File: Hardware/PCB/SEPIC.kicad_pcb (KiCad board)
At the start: 2 copper layers, 33.6 x 35.9 mm, 27 parts, among them Q1 IRF7807, U1 LM3478MA

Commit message: Finished PCB layout
A few minor adjustments still need to be made
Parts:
- added G***: LOGO, Logo_footprint:Logo_10_6, B.Cu at (124.3, 65.1)
- added G***: LOGO, Logo_footprint:Logo_15_15, B.Cu at (110.5, 65.2)
- moved R1 45.6 mm to (99.9, 75.8), turned to 90 degrees
- moved R7 43.7 mm to (124.3, 52.6), turned to 180 degrees
- moved R6 43.0 mm to (119.1, 54.7), turned to 180 degrees
- moved U1 42.5 mm to (124.3, 57.9), turned to 90 degrees
- moved C7 41.9 mm to (120.4, 58.9), turned to -90 degrees
- moved C2 40.7 mm to (105.9, 73.8), turned to -90 degrees
- moved L2 38.1 mm to (118.7, 65.1), turned to -90 degrees
- moved D1 38.0 mm to (99.9, 71.1), turned to 90 degrees
- moved Q1 37.3 mm to (123.3, 74.9), turned to 0 degrees
- moved R4 36.3 mm to (124.1, 69.3)
- moved C1 35.5 mm to (117.9, 58.9), turned to -90 degrees
- moved C5 34.8 mm to (116.8, 70.0), turned to 0 degrees
- moved L1 34.1 mm to (115.0, 74.9), turned to 90 degrees
- moved D4 33.5 mm to (112.3, 67.6), turned to -90 degrees
- moved R2 32.8 mm to (107.9, 64.8), turned to -90 degrees
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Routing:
- net GND: track 0.00 -> 92.7 mm, vias 0 -> 47
- net /Feedback: track 0.00 -> 24.7 mm
- net /DR: track 0.00 -> 23.5 mm, vias 0 -> 2
- net /Isen: track 0.00 -> 20.5 mm, vias 0 -> 2
- net Vin: track 0.00 -> 9.77 mm, vias 0 -> 2
- net Net-(R3-Pad2): track 0.00 -> 7.91 mm
- net Net-(Q1-D): track 0.00 -> 6.24 mm
- net Net-(U1-FA/SD): track 0.00 -> 3.17 mm
- net Net-(U1-COMP): track 0.00 -> 2.88 mm
- net Net-(C6-Pad1): track 0.00 -> 2.41 mm
- net Net-(U1-V_{IN}): track 0.00 -> 2.17 mm
- net Net-(D3-K): track 0.00 -> 1.90 mm
- net Net-(D1-K): track 0.00 -> 1.88 mm
- added copper zone on B.Cu, net GND
- added copper zone on F.Cu, net GND
- added copper zone on F.Cu, net Net-(D4-A)
- added copper zone on F.Cu, net Vin
- added copper zone on F.Cu, net Vout
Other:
- board size 33.6 x 35.9 mm -> 37.5 x 28.5 mm
- board text added: "Boost/Buck DC/DC converter |10/10/2026|"
- board text added: "Vin"
- board text added: "Vin : 3-20 V Vout : 3-20 V Max I : 3 A const."
- board text added: "Vout"

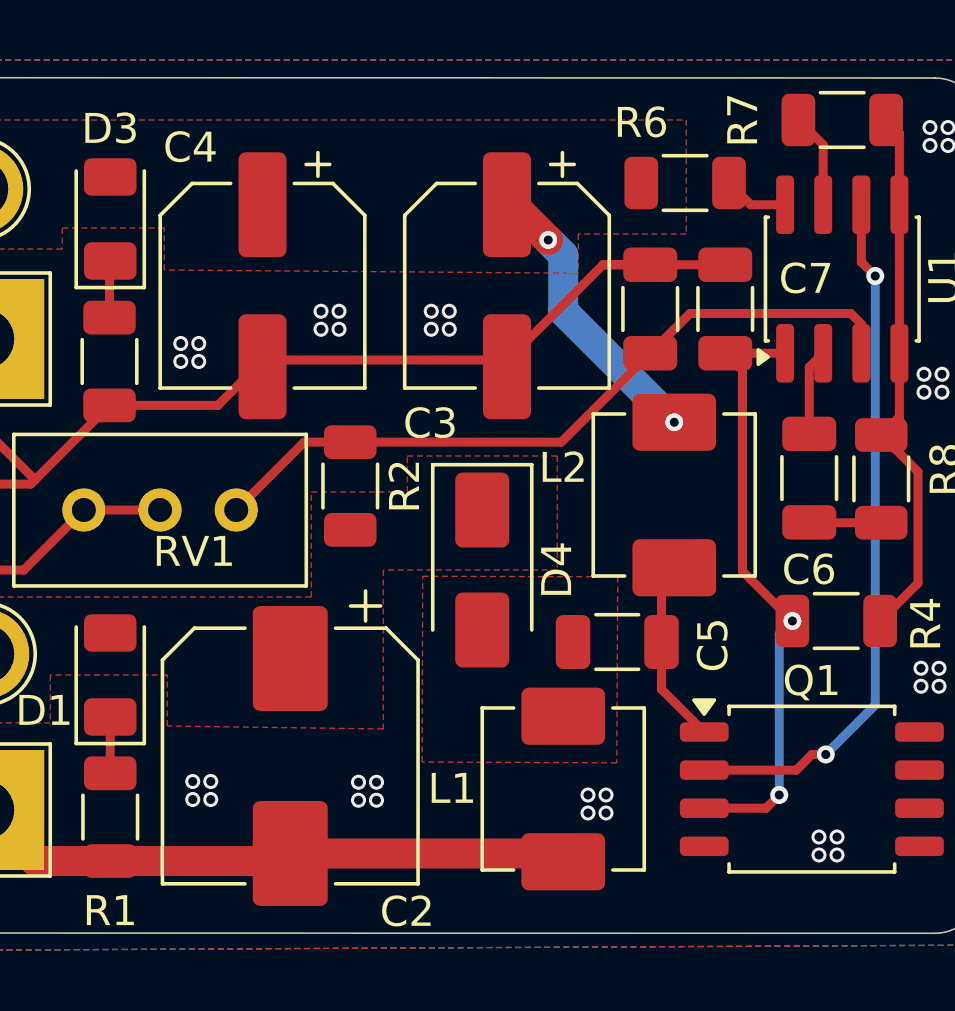
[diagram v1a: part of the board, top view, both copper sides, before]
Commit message: Add C8; update footprints, routing, schematic
Added capacitor C8 (1206) to PCB and schematic and created Hardware/PCB/SEPIC.png. Updated many footprint positions, silk labels and power symbols (#PWR17), adjusted routing (new segments, vias, some trace widths increased), and refined filled copper polygons. Schematic updated with new wires/junctions and an embedded board image. Also changed project prefs (active_layer) and recorded used_designators in .kicad_pro.
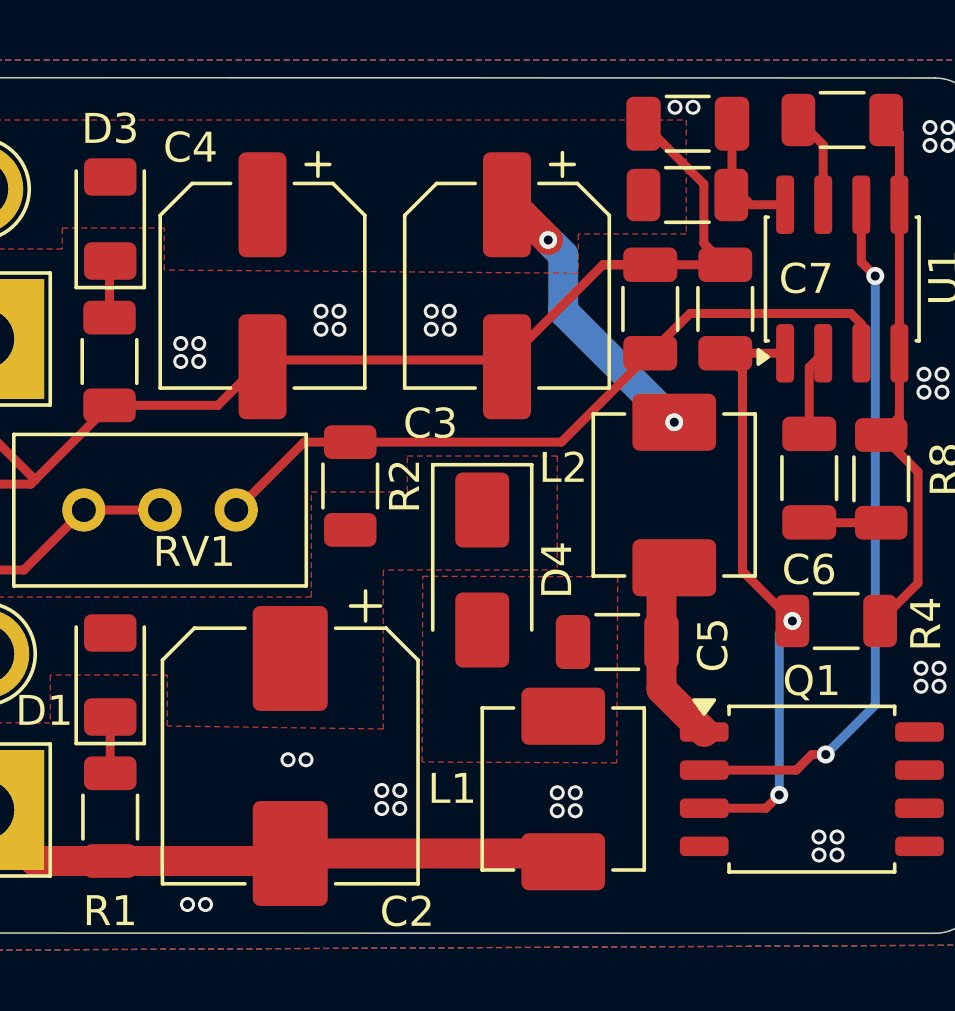
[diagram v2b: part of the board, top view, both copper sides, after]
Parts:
- added C8: 100p, Capacitor_SMD:C_1206_3216Metric, F.Cu at (119.2, 52.7)
- moved G*** 1.92 mm to (112.1, 64.0)
- moved R6 0.41 mm to (119.1, 55.1)
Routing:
- net GND: track 92.7 -> 98.5 mm, vias 47 -> 49
- net Net-(U1-V_{IN}): track 2.17 -> 4.56 mm
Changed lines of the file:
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@@
 		)
 	)
+	(footprint "Capacitor_SMD:C_1206_3216Metric"
+		(layer "F.Cu")
+		(at 119.15 52.725 180)
+		(descr "Capacitor SMD 1206 (3216 Metric), square (rectangular) end terminal, IPC-7351 nominal, (Body size source: IPC-SM-782 page 76, https://www.pcb-3d.com/wordpress/wp-content/uploads/ipc-sm-782a_amendment_1_and_2.pdf)")
+		(tags "capacitor")
+		(property "Reference" "C8"
+			(at -3.1 0.275 270)
+			(layer "B.SilkS")
+			(effects
+				(font
+					(size 1 1)
+					(thickness 0.15)
+				)
+				(justify mirror)
+			)
+		)
+		(property "Value" "100p"
+			(at 0 1.85 0)
+			(layer "F.Fab")
+			(effects
+				(font
+					(size 1 1)
+					(thickness 0.15)
+				)
+			)
+		)
+		(property "Datasheet" ""
+			(at 0 0 0)
+			(layer "F.Fab")
+			(hide yes)
+			(effects
+				(font
+					(size 1.27 1.27)
+				)
+			)
+		)
+		(property "Description" "Unpolarized capacitor"
+			(at 0 0 0)
+			(layer "F.Fab")
+			(hide yes)
+			(effects
+				(font
+					(size 1.27 1.27)
+				)
+			)
+		)
+		(property "KiLib_Generator" "SMD_2terminal_chip_molded"
+			(at 0 0 0)
+			(layer "F.SilkS")
+			(hide yes)
+			(effects
+				(font
+					(size 1 1)
+					(thickness 0.15)
+				)
+			)
+		)
+		(property ki_fp_filters "C_*")
+		(sheetname "/")
+		(sheetfile "SEPIC.kicad_sch")
+		(units
+			(unit
+				(name "A")
+				(pins "1" "2")
+			)
+		)
+		(attr smd)
+		(duplicate_pad_numbers_are_jumpers no)
+		(fp_line
+			(start -0.711252 0.91)
+			(end 0.711252 0.91)
+			(stroke
+				(width 0.12)
+				(type solid)
+			)
+			(layer "F.SilkS")
+		)
+		(fp_line
+			(start -0.711252 -0.91)
+			(end 0.711252 -0.91)
+			(stroke
+				(width 0.12)
+				(type solid)
+			)
+			(layer "F.SilkS")
+		)
+		(fp_rect
+			(start -2.3 -1.15)
+			(end 2.3 1.15)
+			(stroke
+				(width 0.05)
+				(type solid)
+			)
+			(fill no)
+			(layer "F.CrtYd")
+		)
+		(fp_rect
+			(start -1.6 -0.8)
+			(end 1.6 0.8)
+			(stroke
+				(width 0.1)
+				(type solid)
+			)
+			(fill no)
+			(layer "F.Fab")
+		)
+		(fp_text user "${REFERENCE}"
+			(at 0 0 0)
+			(layer "F.Fab")
+			(effects
+				(font
+					(size 0.8 0.8)
+					(thickness 0.12)
+				)
+			)
+		)
+		(pad "1" smd roundrect
+			(at -1.475 0 180)
+			(size 1.15 1.8)
+			(layers "F.Cu" "F.Mask" "F.Paste")
+			(roundrect_rratio 0.217391)
+			(net "Net-(U1-V_{IN})")
+			(pintype "passive")
+		)
+		(pad "2" smd roundrect
+			(at 1.475 0 180)
+			(size 1.15 1.8)
+			(layers "F.Cu" "F.Mask" "F.Paste")
+			(roundrect_rratio 0.217391)
+			(net "GND")
+			(pintype "passive")
+		)
+		(embedded_fonts no)
+		(model "${KICAD10_3DMODEL_DIR}/Capacitor_SMD.3dshapes/C_1206_3216Metric.step"
+			(offset
+				(xyz 0 0 0)
+			)
+			(scale
+				(xyz 1 1 1)
+			)
+			(rotate
+				(xyz 0 0 0)
+			)
+		)
+	)
 	(footprint "Inductor_SMD:L_Vishay_IHLP-2020"
 		(layer "F.Cu")
@@
 		(tags "resistor")
 		(property "Reference" "R7"
-			(at 3.3 0 90)
-			(layer "F.SilkS")
+			(at -1.4 -1.75 180)
+			(layer "B.SilkS")
 			(effects
 				(font
@@
 					(thickness 0.15)
 				)
+				(justify mirror)
 			)
 		)
@@
 	(footprint "Resistor_SMD:R_1206_3216Metric"
 		(layer "F.Cu")
-		(at 119.0625 54.7 180)
+		(at 119.1375 55.1 180)
 		(descr "Resistor SMD 1206 (3216 Metric), square (rectangular) end terminal, IPC-7351 nominal, (Body size source: IPC-SM-782 page 72, https://www.pcb-3d.com/wordpress/wp-content/uploads/ipc-sm-782a_amendment_1_and_2.pdf)")
 		(tags "resistor")
 		(property "Reference" "R6"
-			(at 1.4625 2 0)
-			(layer "F.SilkS")
+			(at -1.0875 -1 180)
+			(layer "B.SilkS")
 			(effects
 				(font
@@
 					(thickness 0.15)
 				)
+				(justify mirror)
 			)
 		)
@@
 		(tags "capacitor")
 		(property "Reference" "C1"
-			(at 0 -0.1 0)
+			(at -0.15 -2.35 0)
 			(layer "B.SilkS")
 			(effects
@@
 	(footprint "Logo_footprint:Logo_15_15"
 		(layer "B.Cu")
-		(at 110.5 65.15 -90)
+		(at 112.075 64.05 -90)
 		(property "Reference" "G***"
 			(at 0 0 90)
@@
 		)
 	)
-	(gr_text "Vin		: 	3-20 V\nVout	:	3-20 V\nMax I	: 	3 A const."
+	(gr_text "Vin		: 	3-20 V\nVout	:	3-20 V\nMax I	:  3 A const."
 		(at 110.775 76.025 0)
 		(layer "B.SilkS" knockout)
@@
 	)
 	(segment
+		(start 119.6875 56.7125)
+		(end 120.4 57.425)
+		(width 0.3)
+		(layer "F.Cu")
+		(net "GND")
+	)
+	(segment
 		(start 94.5 64.7375)
 		(end 97.25 64.7375)
@@
 	)
 	(segment
+		(start 119.6875 54.7375)
+		(end 119.6875 56.7125)
+		(width 0.3)
+		(layer "F.Cu")
+		(net "GND")
+	)
+	(segment
+		(start 117.675 52.725)
+		(end 119.6875 54.7375)
+		(width 0.3)
+		(layer "F.Cu")
+		(net "GND")
+	)
+	(segment
 		(start 95.7 62.9)
 		(end 95.7 59.9)
@@
 	)
 	(via
-		(at 116.425 75.7)
+		(at 115.4 75.625)
 		(size 0.5)
 		(drill 0.3)
@@
 	)
 	(via
-		(at 108.175 74.675)
+		(at 108.95 74.95)
 		(size 0.5)
 		(drill 0.3)
@@
 	)
 	(via
-		(at 103.25 74.65)
+		(at 106.425 73.925)
 		(size 0.5)
 		(drill 0.3)
@@
 	)
 	(via
+		(at 119.325 52.175)
+		(size 0.5)
+		(drill 0.3)
+		(layers "F.Cu" "B.Cu")
+		(net "GND")
+	)
+	(via
 		(at 127.025 61.675)
 		(size 0.5)
@@
 	)
 	(via
-		(at 116.425 75.1)
+		(at 115.4 75.025)
 		(size 0.5)
 		(drill 0.3)
@@
 	)
 	(via
-		(at 108.775 74.675)
+		(at 109.55 74.95)
 		(size 0.5)
 		(drill 0.3)
@@
 	)
 	(via
-		(at 102.65 75.25)
+		(at 102.475 78.75)
 		(size 0.5)
 		(drill 0.3)
@@
 	)
 	(via
-		(at 115.825 75.7)
+		(at 114.8 75.625)
 		(size 0.5)
 		(drill 0.3)
@@
 	)
 	(via
-		(at 108.175 75.275)
+		(at 108.95 75.55)
 		(size 0.5)
 		(drill 0.3)
@@
 	)
 	(via
-		(at 102.65 74.65)
+		(at 105.825 73.925)
 		(size 0.5)
 		(drill 0.3)
@@
 	)
 	(via
-		(at 115.825 75.1)
+		(at 118.725 52.175)
+		(size 0.5)
+		(drill 0.3)
+		(layers "F.Cu" "B.Cu")
+		(net "GND")
+	)
+	(via
+		(at 114.8 75.025)
 		(size 0.5)
 		(drill 0.3)
@@
 	)
 	(via
-		(at 103.25 75.25)
+		(at 103.075 78.75)
 		(size 0.5)
 		(drill 0.3)
@@
 	)
 	(via
-		(at 108.775 75.275)
+		(at 109.55 75.55)
 		(size 0.5)
 		(drill 0.3)
@@
 		(start 118.275 71.575)
 		(end 119.7 73)
-		(width 0.3)
+		(width 1)
 		(layer "F.Cu")
 		(net "Net-(Q1-D)")
@@
 		(start 118.275 70)
 		(end 118.275 67.9505)
-		(width 0.3)
+		(width 1)
 		(layer "F.Cu")
 		(net "Net-(Q1-D)")
@@
 		(start 118.275 70)
 		(end 118.275 71.575)
-		(width 0.3)
+		(width 1)
 		(layer "F.Cu")
 		(net "Net-(Q1-D)")
@@
 	)
 	(segment
+		(start 120.625 52.725)
+		(end 120.625 55.075)
+		(width 0.3)
+		(layer "F.Cu")
+		(net "Net-(U1-V_{IN})")
+	)
+	(segment
 		(start 122.395 55.425)
 		(end 121.25 55.425)
 		(width 0.3)
 		(layer "F.Cu")
+		(net "Net-(U1-V_{IN})")
+	)
+	(segment
+		(start 120.625 55.075)
+		(end 120.6 55.1)
+		(width 0.3)
+		(layer "F.Cu")

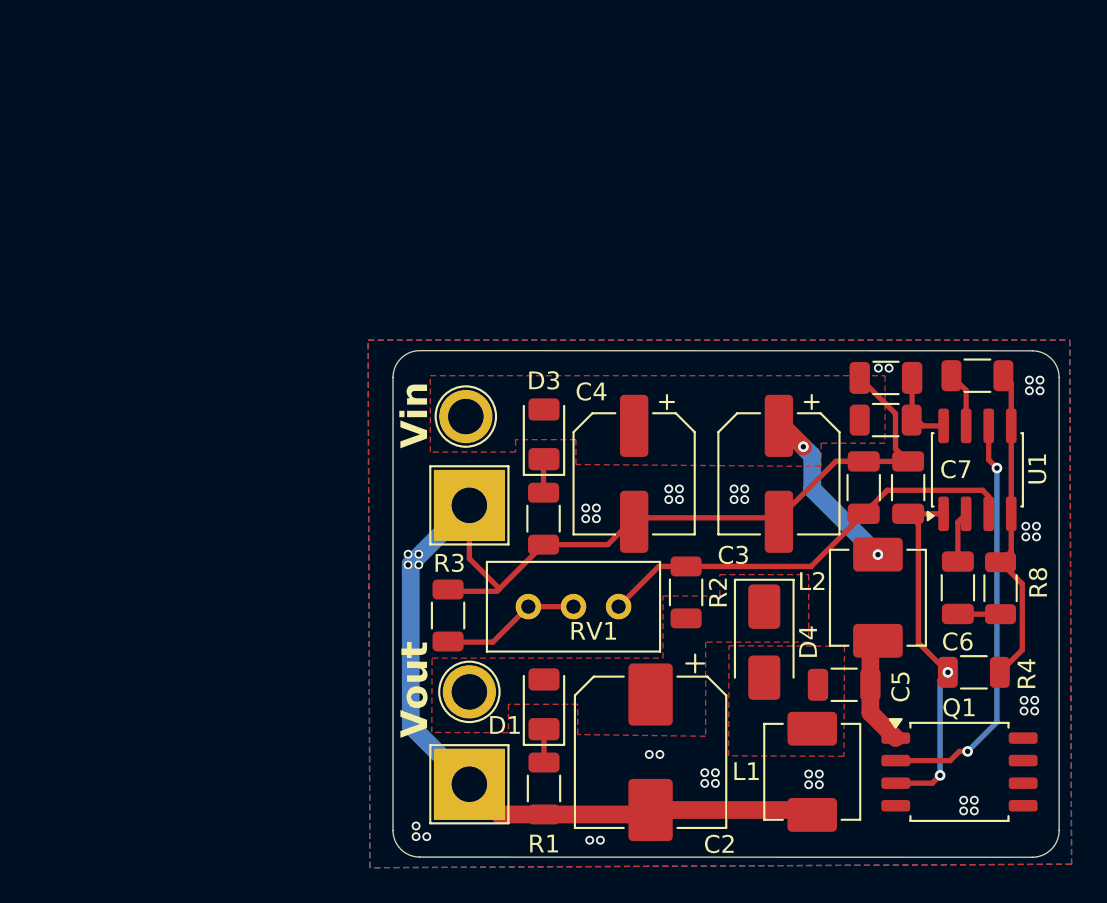
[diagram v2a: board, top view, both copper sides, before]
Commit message: Added reverse voltage protection
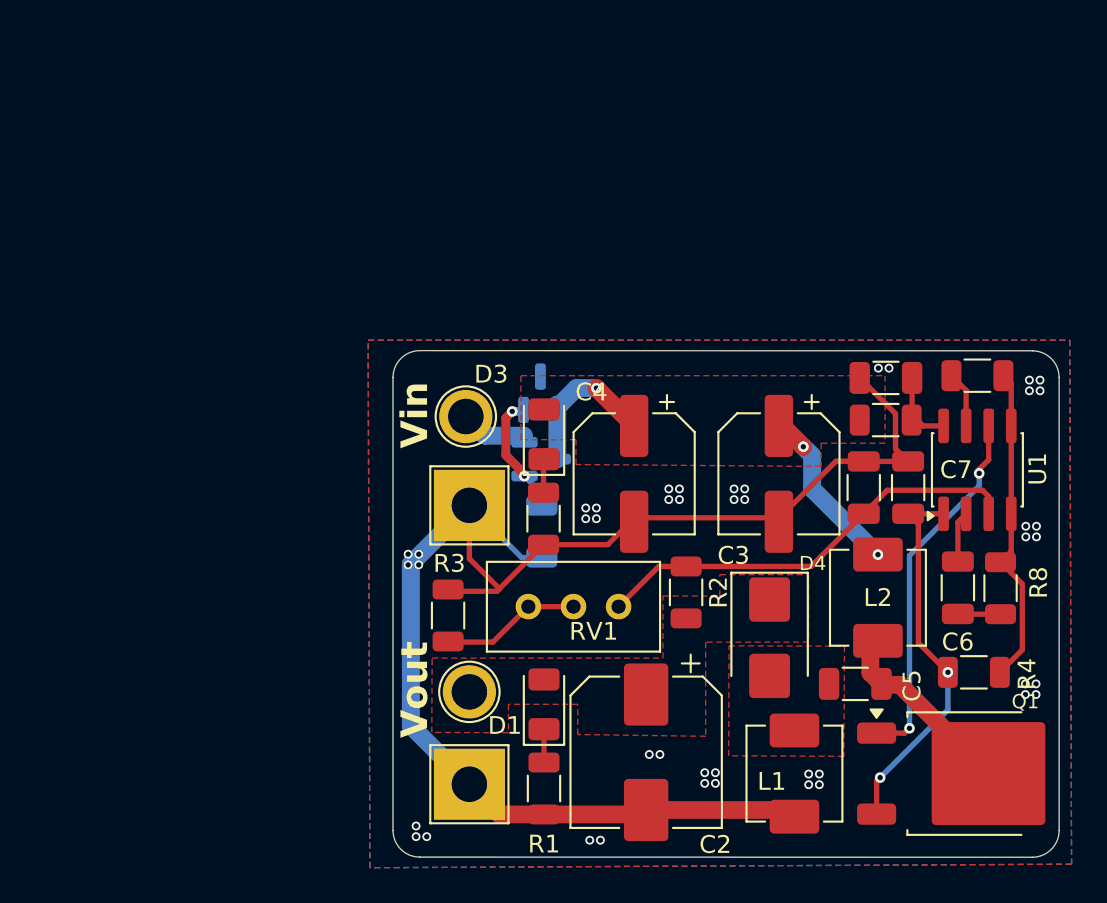
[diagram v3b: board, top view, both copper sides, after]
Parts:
- added D2: BZX84-A10,215, Package_TO_SOT_SMD:SOT-23, B.Cu at (99.7, 53.6)
- added Q2: AO3401A, Package_TO_SOT_SMD:SOT-23, B.Cu at (99.7, 57.3)
- added R9: 1k, Resistor_SMD:R_1206_3216Metric, B.Cu at (99.8, 61.4)
- D4: value SS32 -> STPS3L60U; footprint Diode_SMD:D_SMA -> Diode_SMD:D_SMB
- Q1: value IRF7807 -> IRFR024PBF; footprint Package_SO:SOIC-8_5.3x5.3mm_P1.27mm -> IRFR024:IRFR024PBF
- moved L1 1.00 mm to (114.0, 75.0)
- moved C5 0.63 mm to (117.4, 70.0)
- moved D4 0.39 mm to (112.6, 67.3)
- moved Q1 0.39 mm to (123.7, 75.0)
- moved C2 0.25 mm to (105.7, 73.8)
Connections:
- C3 pad 1: Vin -> /Vbus
- C4 pad 1: Vin -> /Vbus
- D3 pad 2: Vin -> /Vbus
- L2 pad 1: Vin -> /Vbus
- R6 pad 2: Vin -> /Vbus
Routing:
- net /Vbus: track 0.00 -> 18.5 mm, vias 0 -> 3
- net Net-(D2-A): track 0.00 -> 6.93 mm, vias 0 -> 2
- net Vin: track 9.77 -> 3.72 mm, vias 2 -> 0
- net Net-(Q1-D): track 6.24 -> 12.2 mm
- net GND: track 98.5 -> 103.5 mm, vias 49 -> 45
- net /DR: track 23.5 -> 20.8 mm
- net /Isen: track 20.5 -> 21.5 mm
- added copper zone on F.Cu, net /Vbus
- removed copper zone on F.Cu, net Vin

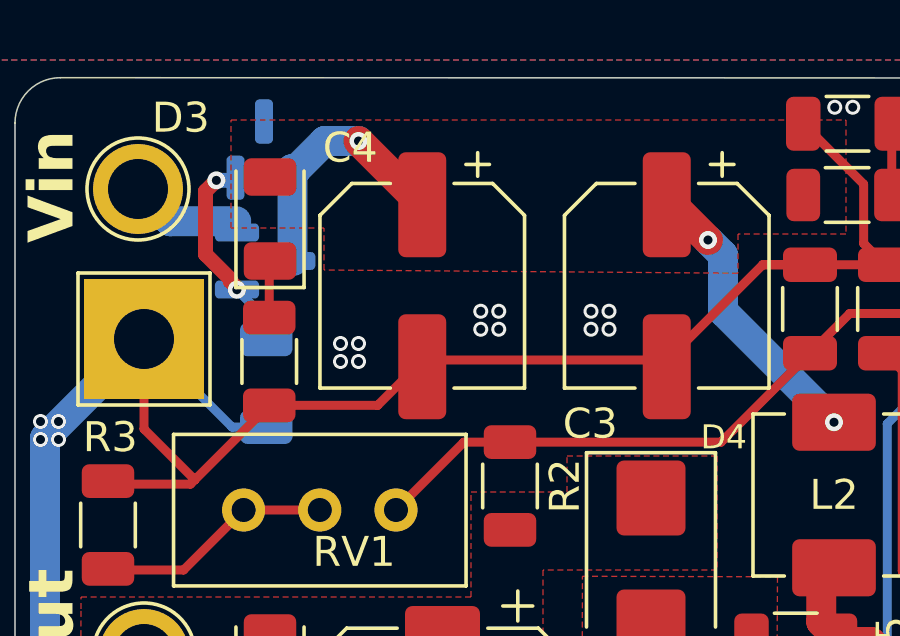
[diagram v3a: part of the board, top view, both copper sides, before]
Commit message: Fixed reverse voltage protection footprints
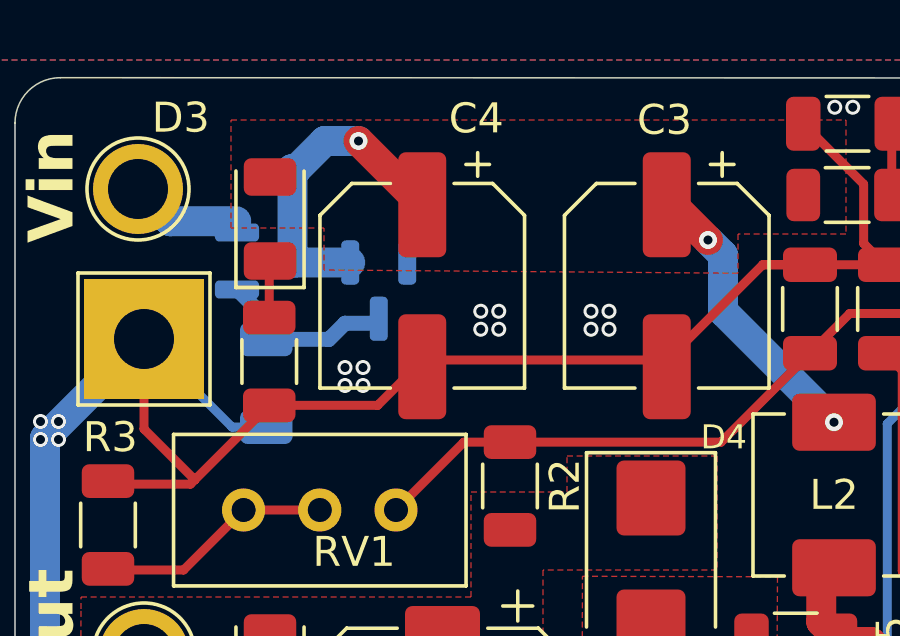
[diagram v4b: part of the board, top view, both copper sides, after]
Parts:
- D2: footprint Package_TO_SOT_SMD:SOT-23 -> BZX84:SOT-23
- moved D2 6.06 mm to (103.5, 58.3), turned to -90 degrees
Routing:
- net /Vbus: track 18.5 -> 20.4 mm
- net Net-(D2-A): track 6.93 -> 6.10 mm, vias 2 -> 0
